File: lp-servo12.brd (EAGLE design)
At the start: 76.1 x 66 mm, 63 parts, among them U1 TPS54526PWP, U2 LMV358

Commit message: Still learning git.  All my files were not in the last commit.
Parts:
- L1: device servoboard:MURATA4900S -> kroesche:VISHAY-IHLP3232DZER
- U1: device servoboard:PWP-R-PDSO-G14 -> kroesche:PWP-R-PDSO-G14
- moved X1 70.0 mm to (72.4, 38.1), turned to 90 degrees
- moved STANDOFF1 48.3 mm to (53.3, 5.08)
- moved STANDOFF2 48.3 mm to (22.9, 5.08)
- moved J10 43.7 mm to (27.9, 2.54), turned to 0 degrees
- moved LOGO2 38.2 mm to (41.9, 36.8)
- moved STANDOFF4 29.0 mm to (53.3, 38.1)
- moved L1 25.4 mm to (48.3, 25.4), turned to 180 degrees
- moved C12 25.4 mm to (29.8, 24.1)
- moved C7 25.4 mm to (41.3, 26.0)
- moved C8 25.4 mm to (30.5, 27.9)
- moved C9 25.4 mm to (39.4, 30.5)
- moved C11 25.4 mm to (27.3, 24.8)
- moved R13 25.4 mm to (27.3, 29.2)
- moved R14 25.4 mm to (24.5, 26.7)
- moved R15 25.4 mm to (29.2, 21.0)
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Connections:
- net GND: now also X1.1; no longer X1.2
- net N$7: now also L1.2; no longer L1.1
- net SERVO_V: now also L1.1; no longer L1.2
- net VBAT: now also X1.2; no longer X1.1
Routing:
- net SERVO_V: track 51.2 -> 5.33 mm
- net GND: track 53.4 -> 69.0 mm, vias 22 -> 25
- net VBAT: track 67.0 -> 76.2 mm, vias 4 -> 3
- net AIN2: track 20.8 -> 23.6 mm, vias 0 -> 2
- net +5V: track 51.0 -> 51.3 mm, vias 2 -> 0
- net N$1: vias 0 -> 2
- net N$3: vias 0 -> 2
- removed copper zone on layer 1, net VBAT
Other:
- board size 76.1 x 66 mm -> 76.1 x 43.2 mm
- board text added: "-BAT+"
- board text added: "12-SERVO"
- board text added: "2013-01"
- board text added: "BOOSTERPACK"
- board text added: "LP-SERVO12 1.0"
- board text added: "STELLARIS"
- board text removed: "12-SERVO STELLARIS BOOSTERPACK"
- board text removed: "BAT+"
- board text removed: "SERVOBOARD 1.0 2013-01"
- board text removed: "VBAT"

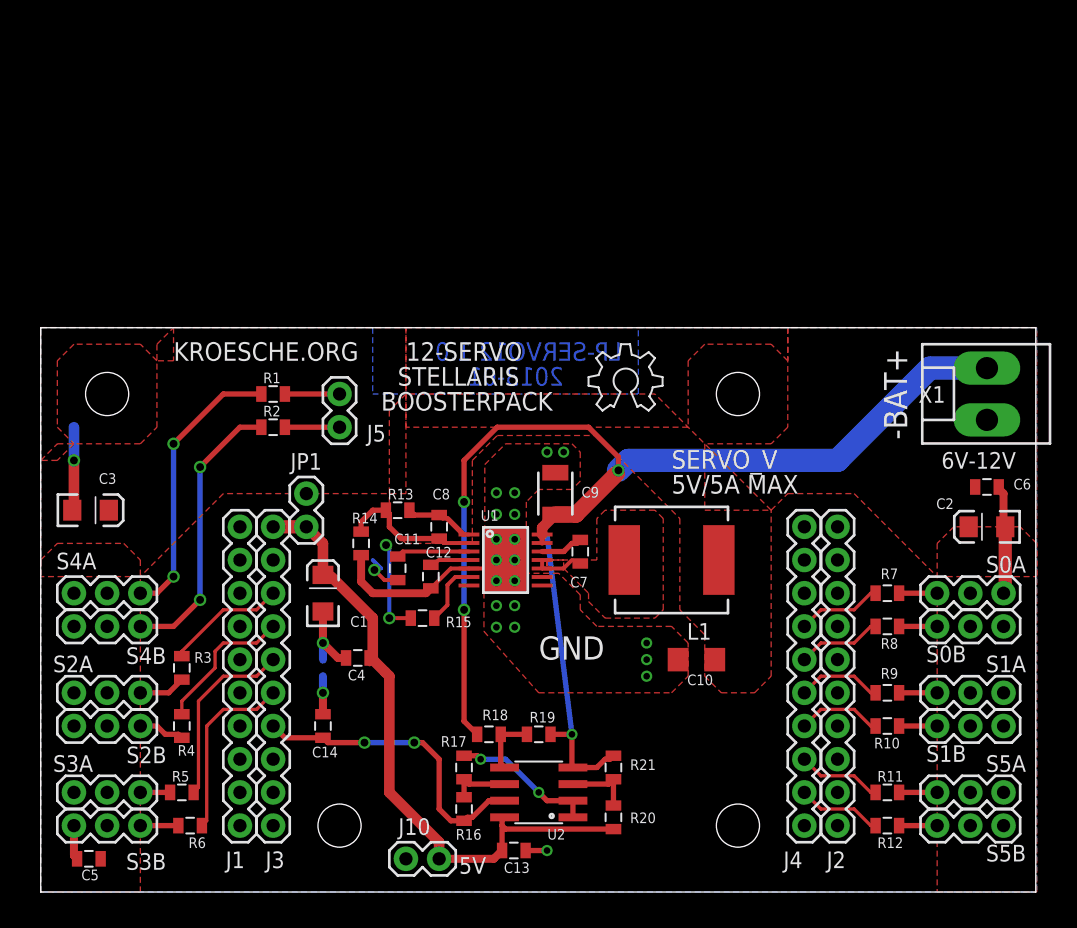
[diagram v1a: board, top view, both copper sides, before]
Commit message: Minor changes to layout.  Moved battery connector so that mounting hole can go in the corner.  Added notes to the bottom silkscreen.
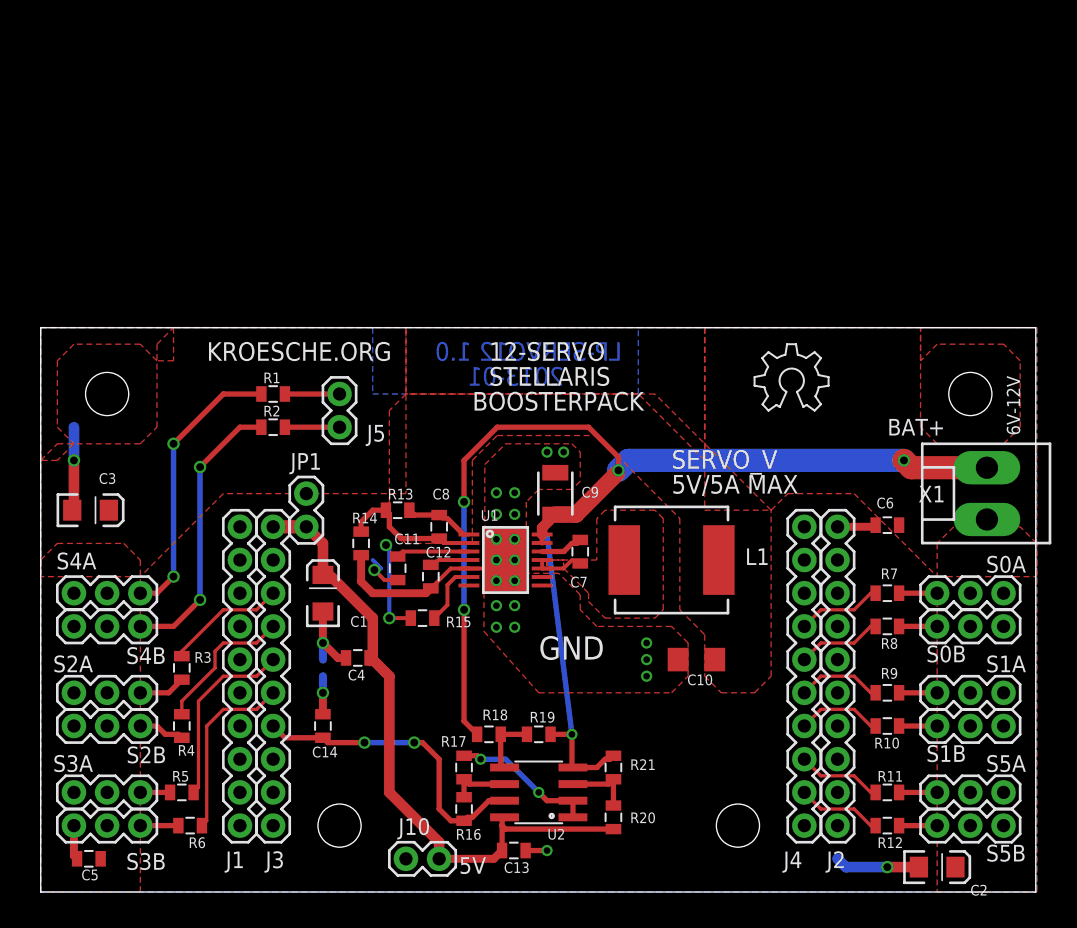
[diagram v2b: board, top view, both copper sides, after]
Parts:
- moved C2 26.3 mm to (68.6, 1.91), turned to 0 degrees
- moved STANDOFF4 17.8 mm to (71.1, 38.1)
- moved LOGO2 12.7 mm to (54.6, 36.8)
- moved C6 8.16 mm to (64.8, 28.1), turned to 180 degrees
- moved X1 7.62 mm to (72.4, 30.5)
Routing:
- net VBAT: track 76.2 -> 73.5 mm, vias 3 -> 4
- net GND: track 69.0 -> 70.1 mm, vias 25 -> 26
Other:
- board text added: "1. CONN X1 IS BATTERY INPUT 6-12V 2. ONBOARD SUPPLY IS 5V/5A 3. JP1 BRIDGED TO POWER LAUNCHPAD+SERVOS 4. JP1 OPEN TO POWER SERVOS ONLY 5. J10 FOR SEPARATE LAUNCHPAD SUPPLY (5V) 6. SxA/B <-> WIDE TIMER xA/B"
- board text added: "BAT+"
- board text added: "NOTES: -----"
- board text removed: "-BAT+"
